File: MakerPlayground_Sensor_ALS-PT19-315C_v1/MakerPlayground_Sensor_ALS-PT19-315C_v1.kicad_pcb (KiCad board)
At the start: 2 copper layers, 30.4 x 19.9 mm, 6 parts, among them J1 Conn_01x04, Q1 Q_Photo_NPN_CE

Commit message: Fix MP Light sensor silk screen.
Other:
- board text removed: "v3.0"
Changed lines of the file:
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@@
   (general
     (thickness 1.6)
-    (drawings 224)
+    (drawings 223)
     (tracks 14)
     (zones 0)
@@
   (gr_line (start 142.156 85.1702) (end 142.08 85.1338) (layer Edge.Cuts) (width 0.1))
   (gr_line (start 139.5 85) (end 138.881 85) (layer Edge.Cuts) (width 0.1))
-  (gr_text v3.0 (at 138.25 103.75) (layer F.SilkS)
-    (effects (font (size 0.5 0.5) (thickness 0.1)))
-  )
   (gr_text Light (at 136.25 102.25) (layer F.SilkS)
     (effects (font (size 1.5 1.5) (thickness 0.3)))

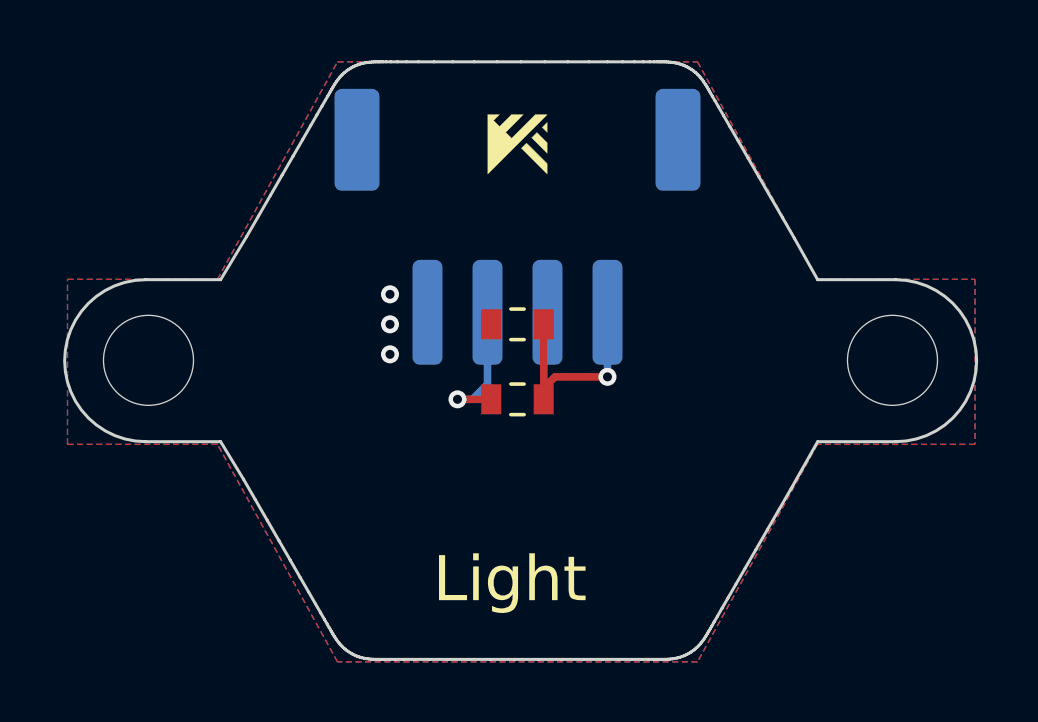
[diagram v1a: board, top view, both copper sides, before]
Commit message: Single HEX design; Lock mounting hole footprint & review mounting hole position.
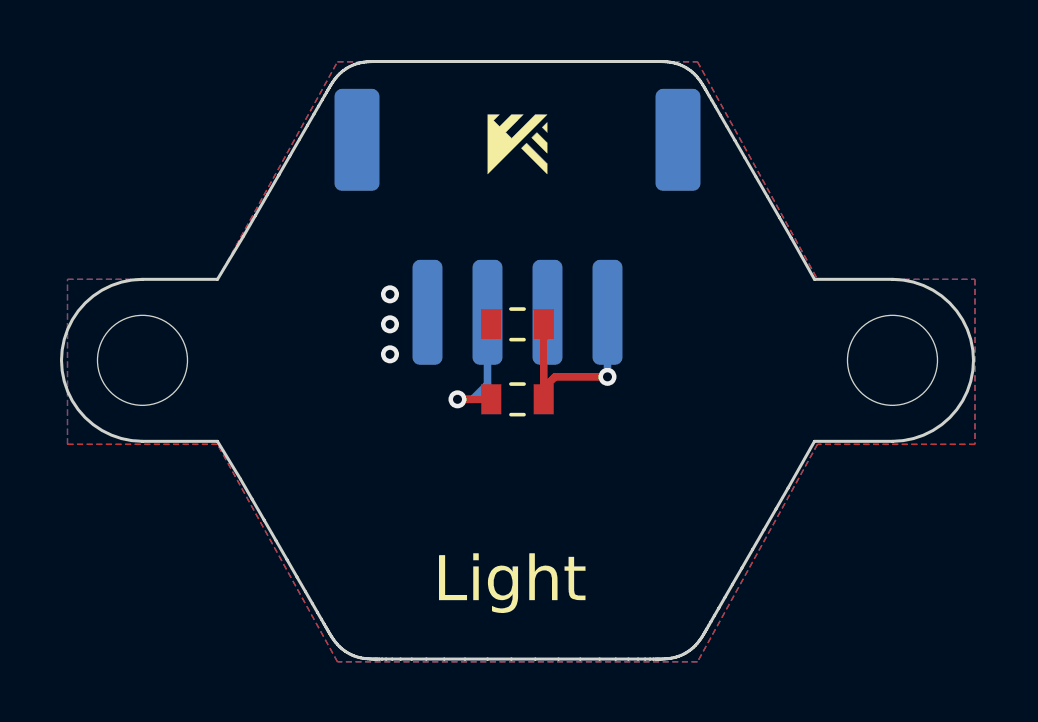
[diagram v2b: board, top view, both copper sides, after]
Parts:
- moved REF** 0.20 mm to (124.0, 95.0)
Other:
- outline, holes or cut-outs redrawn

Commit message: Design complete.
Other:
- board text added: "v1.0"
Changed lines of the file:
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@@
   (general
     (thickness 1.6)
-    (drawings 223)
+    (drawings 224)
     (tracks 14)
     (zones 0)
@@
     (pad 1 np_thru_hole circle (at 0 0) (size 3 3) (drill 3) (layers *.Cu *.Mask))
   )
+  (gr_text v1.0 (at 138.25 104) (layer F.SilkS)
+    (effects (font (size 0.5 0.5) (thickness 0.1)))
+  )
   (gr_line (start 141.232 104.907) (end 141.285 104.907) (layer Edge.Cuts) (width 0.1))
